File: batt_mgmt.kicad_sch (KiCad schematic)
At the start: 49 parts, among them Q1 DMN2014LHAB-7, Q2 DMP3056L, U1 BQ24074RGT, U2 BQ29728, U3 BQ27427

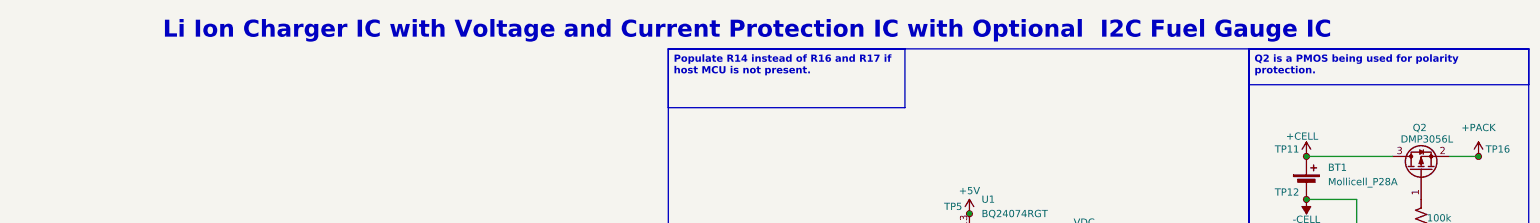
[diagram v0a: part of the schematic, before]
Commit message: Added Graph & cleaned up title and layout
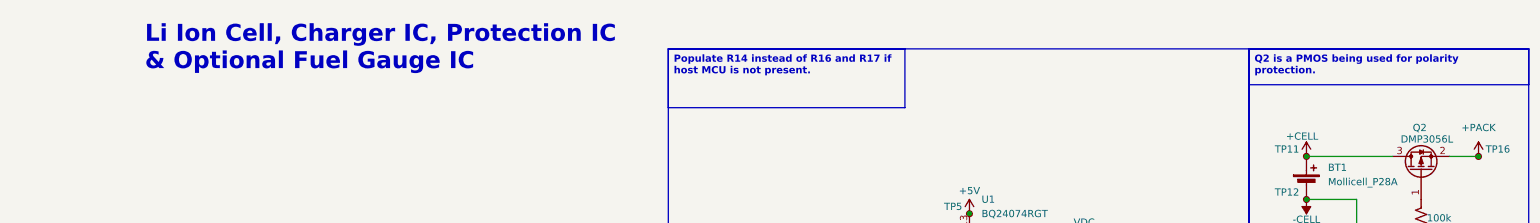
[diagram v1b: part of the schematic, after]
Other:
- note added: "Li Ion Cell, Charger IC, Protection IC & Optional Fuel Gauge IC"
- note removed: "Li Ion Charger IC with Voltage and Current Protection IC with Optional I2C Fuel Gauge IC"
- company: FETfox -> github.com/FETfox/Li-Ion_Power_Module
- title: Li Lion Power Module -> Li Lion Power Module w/ Optional Fuel Gauge &CAN Bus
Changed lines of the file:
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@@
 	(paper "USLetter")
 	(title_block
-		(title "Li Lion Power Module")
-		(date "2026-04-13")
-		(rev "RevB")
-		(company "FETfox")
-		(comment 1 "W/ optional CAN bus interface & I2C fuel gauge.")
+		(title "Li Lion Power Module w/ Optional Fuel Gauge &CAN Bus")
+		(date "2026-06-25")
+		(rev "RevA")
+		(company "github.com/FETfox/Li-Ion_Power_Module")
 	)
 	(rectangle
@@
 		)
 	)
-	(text "Li Ion Charger IC with Voltage and Current Protection IC with Optional  I2C Fuel Gauge IC"
+	(text "Li Ion Cell, Charger IC, Protection IC \n& Optional Fuel Gauge IC"
 		(exclude_from_sim no)
-		(at 120.65 17.018 0)
+		(at 13.97 16.002 0)
 		(effects
 			(font
@@
 				(bold yes)
 			)
+			(justify left top)
 		)
 	)
